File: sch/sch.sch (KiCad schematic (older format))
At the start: 67 parts, among them P1 CONN_01X02, P10 CONN_1, P11 CONN_1, P2 CONN_02X05, P3 CONN_01X06, P4 CONN_01X06, P5 BNC, P6 Digital, P7 Analog, P8 CONN_1, P9 CONN_1, U1 PT4115, U10 DS18B20, U11 DS18B20, U2 PT4115, U3 PT4115, U4 PT4115, U5 PT4115, U6 PT4115, U7 LM324, U8 SALINITY_AND_LEVEL_SENSOR, U9 LM7805CT

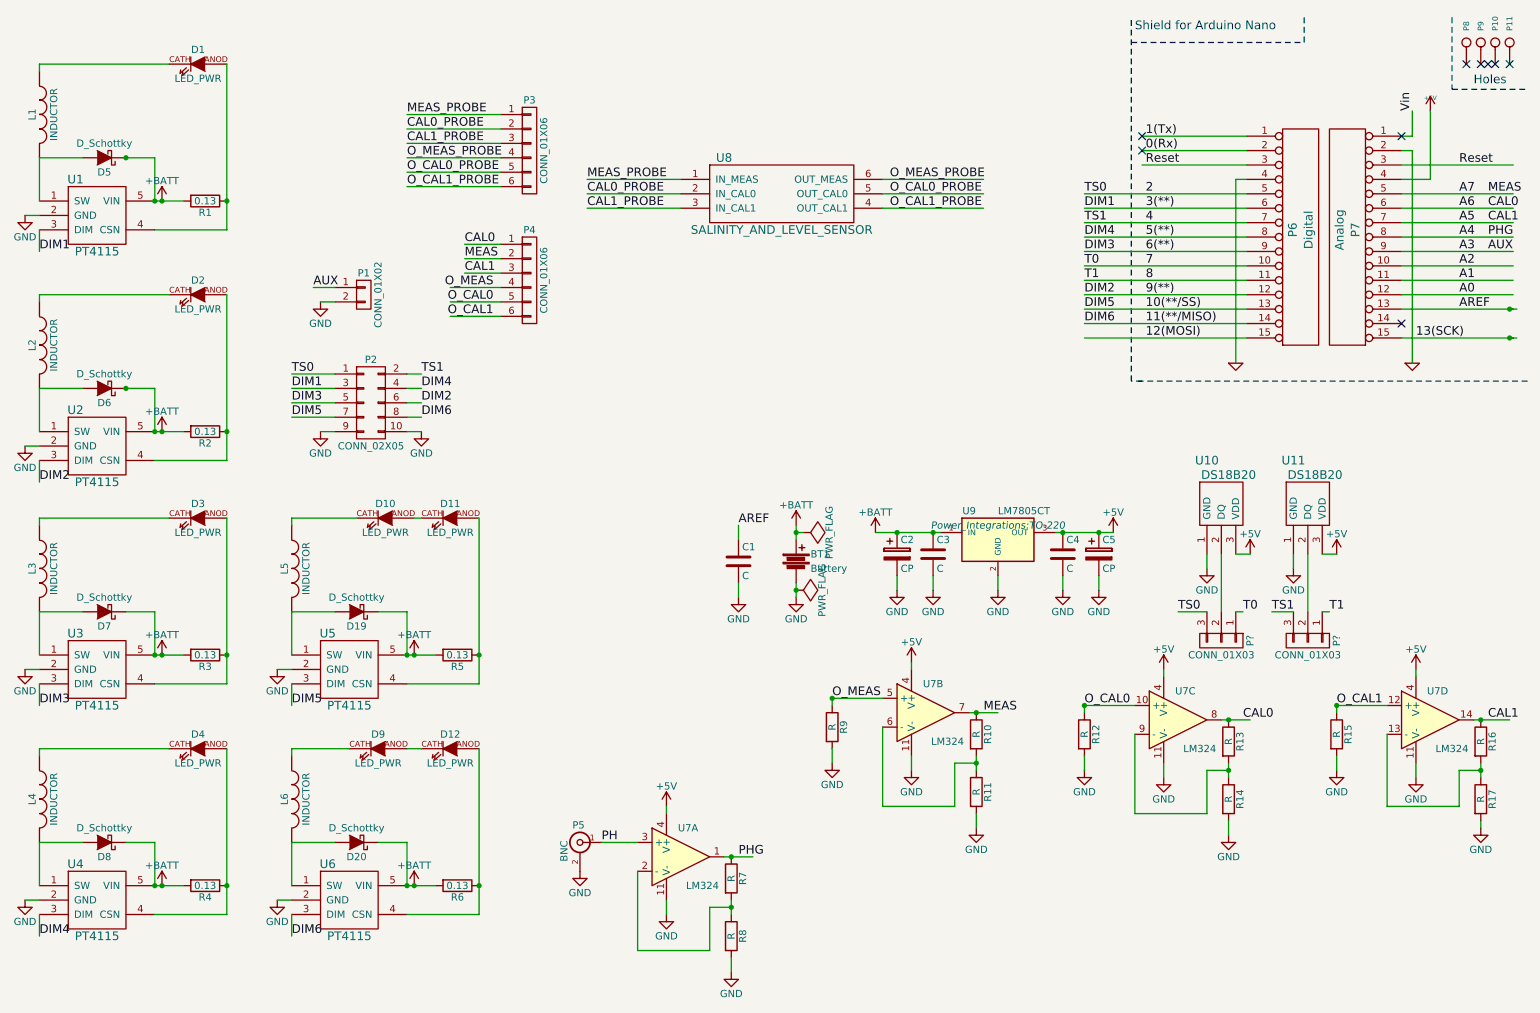
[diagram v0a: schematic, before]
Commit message: Initial version done
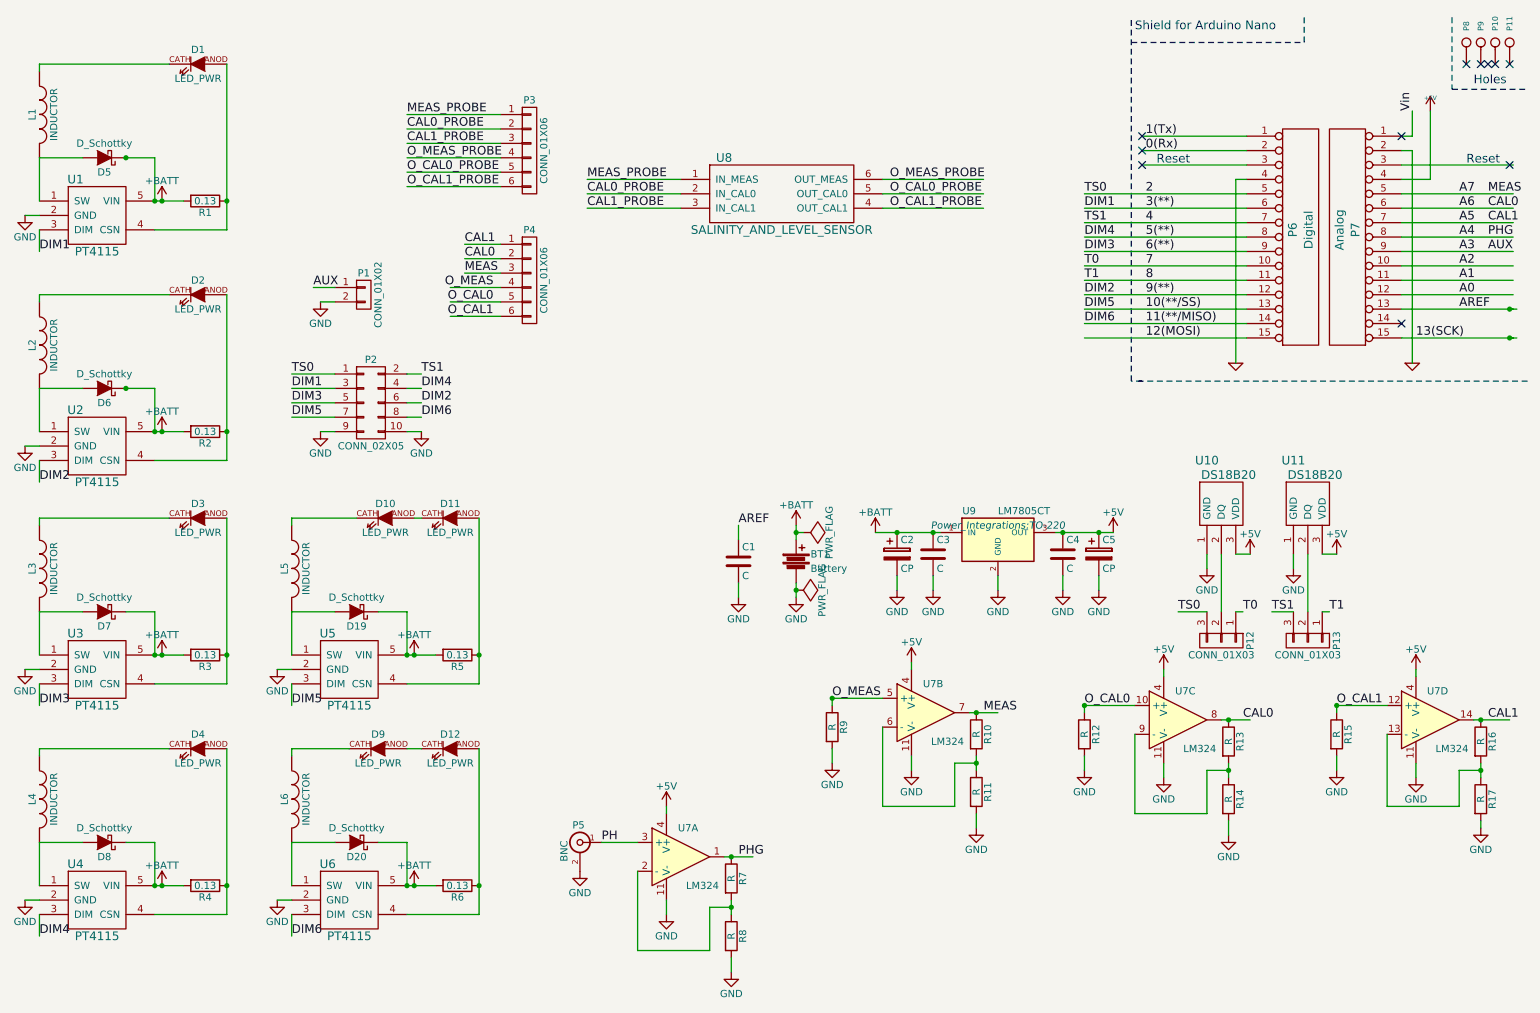
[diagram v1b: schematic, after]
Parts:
- P12, P13: renamed from P?; footprint (none) -> Connect:PINHEAD1-3
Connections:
- net labels removed: Reset
- no-connect marks 9 -> 11
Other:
- note added: "Reset"
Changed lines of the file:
@@
 	1    0    0    -1
 $EndComp
-Text Label 8575 1500 0    60   ~ 0
-Reset
 Text Label 8575 1700 0    60   ~ 0
 2
@@
 	1    0    0    -1
 $EndComp
-Text Label 10750 1500 0    60   ~ 0
-Reset
 Text Notes 10850 950  0    60   ~ 0
 Holes
@@
 	2950 3250 2650 3250
 $Comp
-L GND #PWR044
+L GND #PWR040
 U 1 1 579634D2
 P 3550 3350
-F 0 "#PWR044" H 3550 3100 50  0001 C CNN
+F 0 "#PWR040" H 3550 3100 50  0001 C CNN
 F 1 "GND" H 3550 3200 50  0000 C CNN
 F 2 "" H 3550 3350 50  0000 C CNN
@@
 Connection ~ 1500 1450
 $Comp
-L PWR_FLAG #FLG045
+L PWR_FLAG #FLG041
 U 1 1 57969605
 P 6200 4050
-F 0 "#FLG045" H 6200 4145 50  0001 C CNN
+F 0 "#FLG041" H 6200 4145 50  0001 C CNN
 F 1 "PWR_FLAG" H 6200 4230 50  0000 C CNN
 F 2 "" H 6200 4050 50  0000 C CNN
@@
 	900  5000 800  5000
 $Comp
-L PWR_FLAG #FLG046
+L PWR_FLAG #FLG042
 U 1 1 57957B81
 P 6150 4450
-F 0 "#FLG046" H 6150 4545 50  0001 C CNN
+F 0 "#FLG042" H 6150 4545 50  0001 C CNN
 F 1 "PWR_FLAG" H 6150 4630 50  0000 C CNN
 F 2 "" H 6150 4450 50  0000 C CNN
@@
 Wire Wire Line
 	4100 2250 3850 2250
+Text Label 3850 2250 0    60   ~ 0
+MEAS
 Text Label 3850 2150 0    60   ~ 0
-MEAS
+CAL0
 Text Label 3850 2050 0    60   ~ 0
-CAL0
-Text Label 3850 2250 0    60   ~ 0
 CAL1
 $Comp
@@
 $EndComp
 $Comp
-L GND #PWR047
+L GND #PWR043
 U 1 1 57968DE9
 P 5750 4500
-F 0 "#PWR047" H 5750 4250 50  0001 C CNN
+F 0 "#PWR043" H 5750 4250 50  0001 C CNN
 F 1 "GND" H 5750 4350 50  0000 C CNN
 F 2 "" H 5750 4500 50  0000 C CNN
@@
 $EndComp
 $Comp
-L GND #PWR048
+L GND #PWR044
 U 1 1 5796B122
 P 2850 2450
-F 0 "#PWR048" H 2850 2200 50  0001 C CNN
+F 0 "#PWR044" H 2850 2200 50  0001 C CNN
 F 1 "GND" H 2850 2300 50  0000 C CNN
 F 2 "" H 2850 2450 50  0000 C CNN
@@
 	6750 1600 7450 1600
 $Comp
-L +BATT #PWR049
+L +BATT #PWR045
 U 1 1 57975E0D
 P 6150 4000
-F 0 "#PWR049" H 6150 3850 50  0001 C CNN
+F 0 "#PWR045" H 6150 3850 50  0001 C CNN
 F 1 "+BATT" H 6150 4140 50  0000 C CNN
 F 2 "" H 6150 4000 50  0000 C CNN
@@
 $EndComp
 $Comp
-L +BATT #PWR050
+L +BATT #PWR046
 U 1 1 57975F58
 P 6700 4050
-F 0 "#PWR050" H 6700 3900 50  0001 C CNN
+F 0 "#PWR046" H 6700 3900 50  0001 C CNN
 F 1 "+BATT" H 6700 4190 50  0000 C CNN
 F 2 "" H 6700 4050 50  0000 C CNN
@@
 	3950 6700 3450 6700
 $Comp
-L +5V #PWR051
+L +5V #PWR047
 U 1 1 579871A7
 P 5250 5950
-F 0 "#PWR051" H 5250 5800 50  0001 C CNN
+F 0 "#PWR047" H 5250 5800 50  0001 C CNN
 F 1 "+5V" H 5250 6090 50  0000 C CNN
 F 2 "" H 5250 5950 50  0000 C CNN
@@
 $EndComp
 $Comp
-L +5V #PWR052
+L +5V #PWR048
 U 1 1 57987360
 P 10450 5000
-F 0 "#PWR052" H 10450 4850 50  0001 C CNN
+F 0 "#PWR048" H 10450 4850 50  0001 C CNN
 F 1 "+5V" H 10450 5140 50  0000 C CNN
 F 2 "" H 10450 5000 50  0000 C CNN
@@
 $EndComp
 $Comp
-L +5V #PWR053
+L +5V #PWR049
 U 1 1 5798743D
 P 8700 5000
-F 0 "#PWR053" H 8700 4850 50  0001 C CNN
+F 0 "#PWR049" H 8700 4850 50  0001 C CNN
 F 1 "+5V" H 8700 5140 50  0000 C CNN
 F 2 "" H 8700 5000 50  0000 C CNN
@@
 $EndComp
 $Comp
-L +5V #PWR054
+L +5V #PWR050
 U 1 1 5798751A
 P 6950 4950
-F 0 "#PWR054" H 6950 4800 50  0001 C CNN
+F 0 "#PWR050" H 6950 4800 50  0001 C CNN
 F 1 "+5V" H 6950 5090 50  0000 C CNN
 F 2 "" H 6950 4950 50  0000 C CNN
@@
 $EndComp
 $Comp
-L CONN_01X03 P?
+L CONN_01X03 P12
 U 1 1 57B3E354
 P 9100 4800
-F 0 "P?" H 9100 5000 50  0000 C CNN
+F 0 "P12" H 9100 5000 50  0000 C CNN
 F 1 "CONN_01X03" V 9200 4800 50  0000 C CNN
-F 2 "" H 9100 4800 50  0000 C CNN
+F 2 "Connect:PINHEAD1-3" H 9100 4800 50  0001 C CNN
 F 3 "" H 9100 4800 50  0000 C CNN
 	1    9100 4800
@@
 $EndComp
 $Comp
-L CONN_01X03 P?
+L CONN_01X03 P13
 U 1 1 57B3E4BD
 P 9700 4800
-F 0 "P?" H 9700 5000 50  0000 C CNN
+F 0 "P13" H 9700 5000 50  0000 C CNN
 F 1 "CONN_01X03" V 9800 4800 50  0000 C CNN
-F 2 "" H 9700 4800 50  0000 C CNN
+F 2 "Connect:PINHEAD1-3" H 9700 4800 50  0001 C CNN
 F 3 "" H 9700 4800 50  0000 C CNN
 	1    9700 4800
@@
 Wire Wire Line
 	9000 4600 8800 4600
+NoConn ~ 8550 1500
+NoConn ~ 11100 1500
+Text Notes 8650 1500 0    60   ~ 0
+Reset
+Text Notes 10800 1500 0    60   ~ 0
+Reset
 $EndSCHEMATC

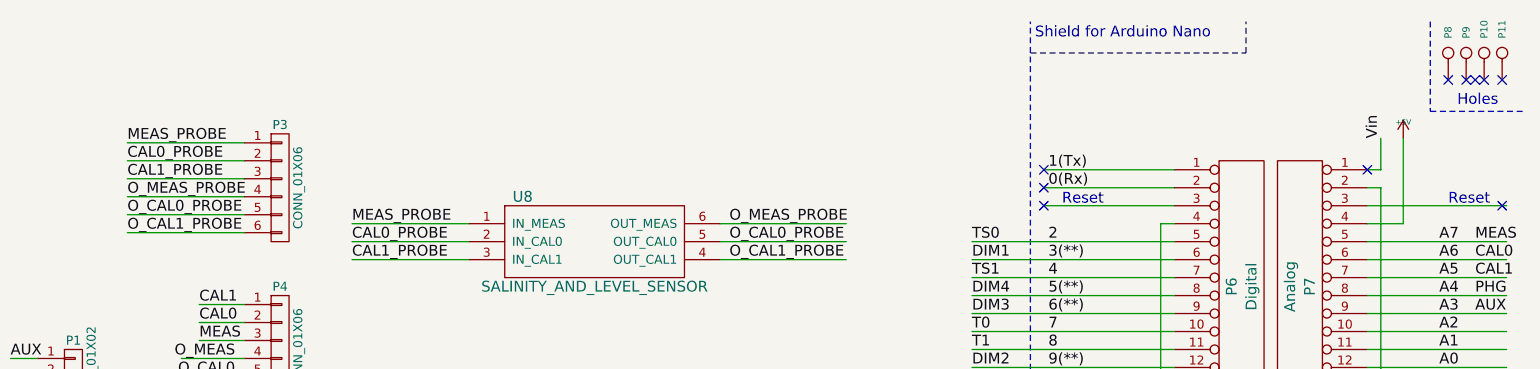
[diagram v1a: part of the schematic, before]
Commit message: Fixed minor details in pcb and added openings in solder mas for thermal vias behind led
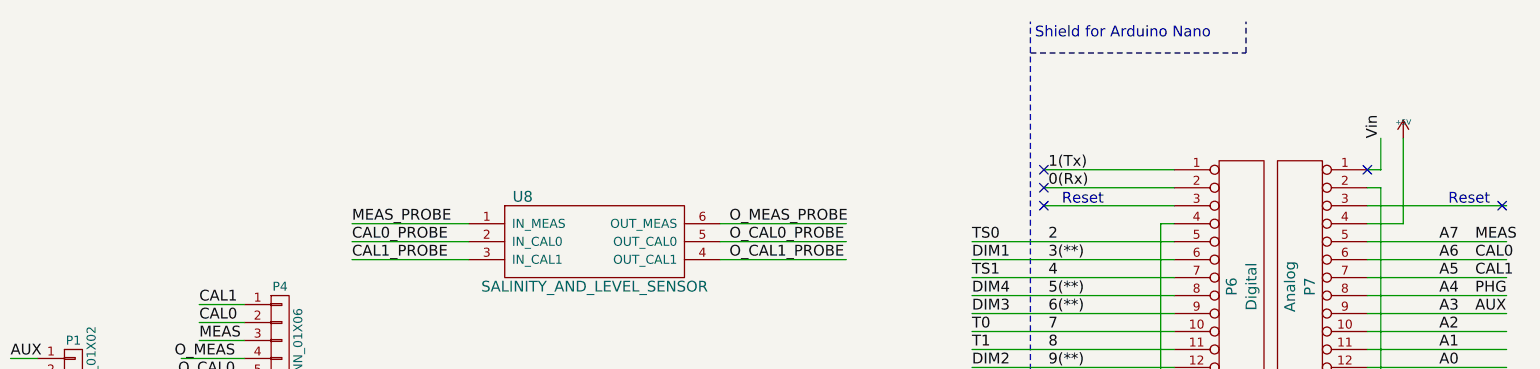
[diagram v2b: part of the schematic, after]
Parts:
- removed P10, P11, P8, P9: CONN_1, Socket_Arduino_Nano:1pin_Nano, symbol CONN_1
- removed P3: CONN_01X06, Connect:PINHEAD1-6, symbol CONN_01X06
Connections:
- wire segments 201 -> 195
- no-connect marks 11 -> 6
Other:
- note removed: "Holes"
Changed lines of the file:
@@
 $EndDescr
-$Comp
-L CONN_1 P8
-U 1 1 551D9380
-P 10800 650
-F 0 "P8" H 10880 650 40  0000 L CNN
-F 1 "CONN_1" H 10800 705 30  0001 C CNN
-F 2 "Socket_Arduino_Nano:1pin_Nano" H 10800 650 60  0001 C CNN
-F 3 "" H 10800 650 60  0000 C CNN
-	1    10800 650
-	0    -1   -1   0
-$EndComp
-$Comp
-L CONN_1 P9
-U 1 1 551D9414
-P 10900 650
-F 0 "P9" H 10980 650 40  0000 L CNN
-F 1 "CONN_1" H 10900 705 30  0001 C CNN
-F 2 "Socket_Arduino_Nano:1pin_Nano" H 10900 650 60  0001 C CNN
-F 3 "" H 10900 650 60  0000 C CNN
-	1    10900 650
-	0    -1   -1   0
-$EndComp
-$Comp
-L CONN_1 P10
-U 1 1 551D9432
-P 11000 650
-F 0 "P10" H 11080 650 40  0000 L CNN
-F 1 "CONN_1" H 11000 705 30  0001 C CNN
-F 2 "Socket_Arduino_Nano:1pin_Nano" H 11000 650 60  0001 C CNN
-F 3 "" H 11000 650 60  0000 C CNN
-	1    11000 650
-	0    -1   -1   0
-$EndComp
-$Comp
-L CONN_1 P11
-U 1 1 551D9466
-P 11100 650
-F 0 "P11" H 11180 650 40  0000 L CNN
-F 1 "CONN_1" H 11100 705 30  0001 C CNN
-F 2 "Socket_Arduino_Nano:1pin_Nano" H 11100 650 60  0001 C CNN
-F 3 "" H 11100 650 60  0000 C CNN
-	1    11100 650
-	0    -1   -1   0
-$EndComp
 $Comp
 L CONN_15 P6
@@
 	-1   0    0    -1
 $EndComp
-NoConn ~ 10800 800
-NoConn ~ 10900 800
-NoConn ~ 11000 800
-NoConn ~ 11100 800
 Text Label 8575 1300 0    60   ~ 0
 1(Tx)
@@
 	1    0    0    -1
 $EndComp
-Text Notes 10850 950  0    60   ~ 0
-Holes
 Text Notes 8500 575  0    60   ~ 0
 Shield for Arduino Nano
@@
 Wire Wire Line
 	10350 1600 10550 1600
-Wire Notes Line
-	10700 475  10700 975
-Wire Notes Line
-	10700 975  11225 975
 Wire Wire Line
 	10550 1600 10550 1125
@@
 NoConn ~ 8550 1300
 NoConn ~ 8550 1400
-NoConn ~ 10950 800
 Connection ~ 1500 1450
 $Comp
@@
 	1    0    0    -1
 $EndComp
-$Comp
-L CONN_01X06 P3
-U 1 1 5796C595
-P 4300 1400
-F 0 "P3" H 4300 1750 50  0000 C CNN
-F 1 "CONN_01X06" V 4400 1400 50  0000 C CNN
-F 2 "Connect:PINHEAD1-6" H 4300 1400 50  0001 C CNN
-F 3 "" H 4300 1400 50  0000 C CNN
-	1    4300 1400
-	1    0    0    -1
-$EndComp
-Text Label 3450 1450 0    60   ~ 0
-O_MEAS_PROBE
-Text Label 3450 1550 0    60   ~ 0
-O_CAL0_PROBE
-Text Label 3450 1650 0    60   ~ 0
-O_CAL1_PROBE
-Wire Wire Line
-	3450 1650 4100 1650
-Wire Wire Line
-	3450 1550 4100 1550
-Wire Wire Line
-	3450 1450 4100 1450
-Wire Wire Line
-	4100 1150 3450 1150
-Wire Wire Line
-	4100 1250 3450 1250
-Wire Wire Line
-	4100 1350 3450 1350
-Text Label 3450 1150 0    60   ~ 0
-MEAS_PROBE
-Text Label 3450 1250 0    60   ~ 0
-CAL0_PROBE
-Text Label 3450 1350 0    60   ~ 0
-CAL1_PROBE
 Wire Wire Line
 	5350 1600 4700 1600
